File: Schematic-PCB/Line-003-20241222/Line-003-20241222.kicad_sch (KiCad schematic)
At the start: 223 parts, among them J1 VIN, J2 Conn_MD, SW1 RESET, U47 LM393, U48 LM393, U49 LM393, U50 LM393, U51 LM393, U52 LM393, U53 LM393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

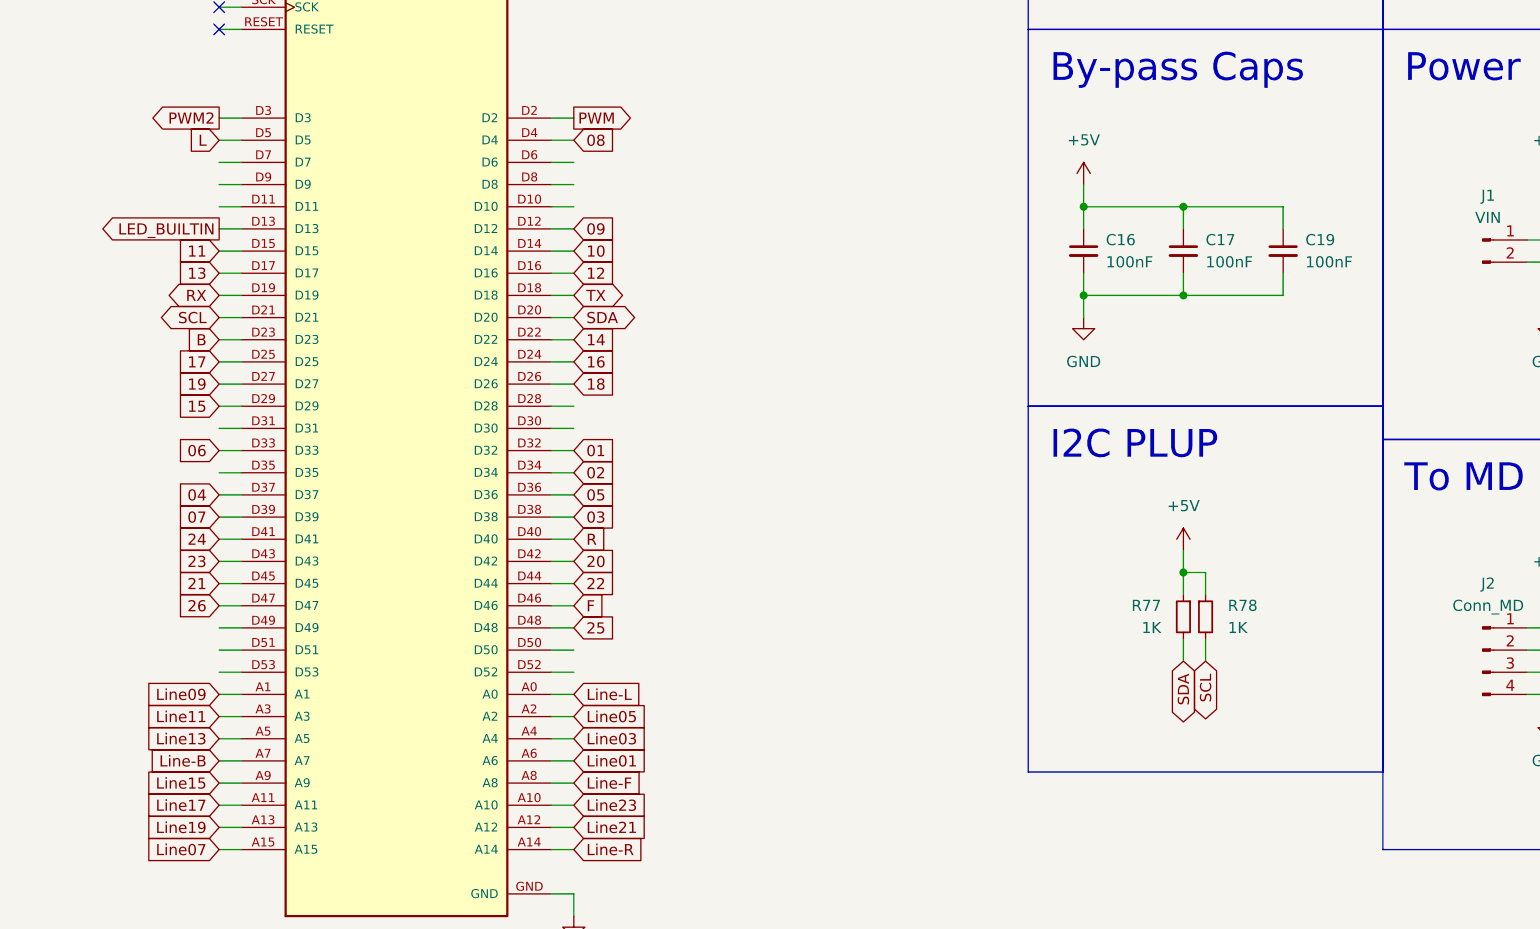
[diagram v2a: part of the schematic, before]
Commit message: update: ラインセンサ基板の2次DRを完了させた
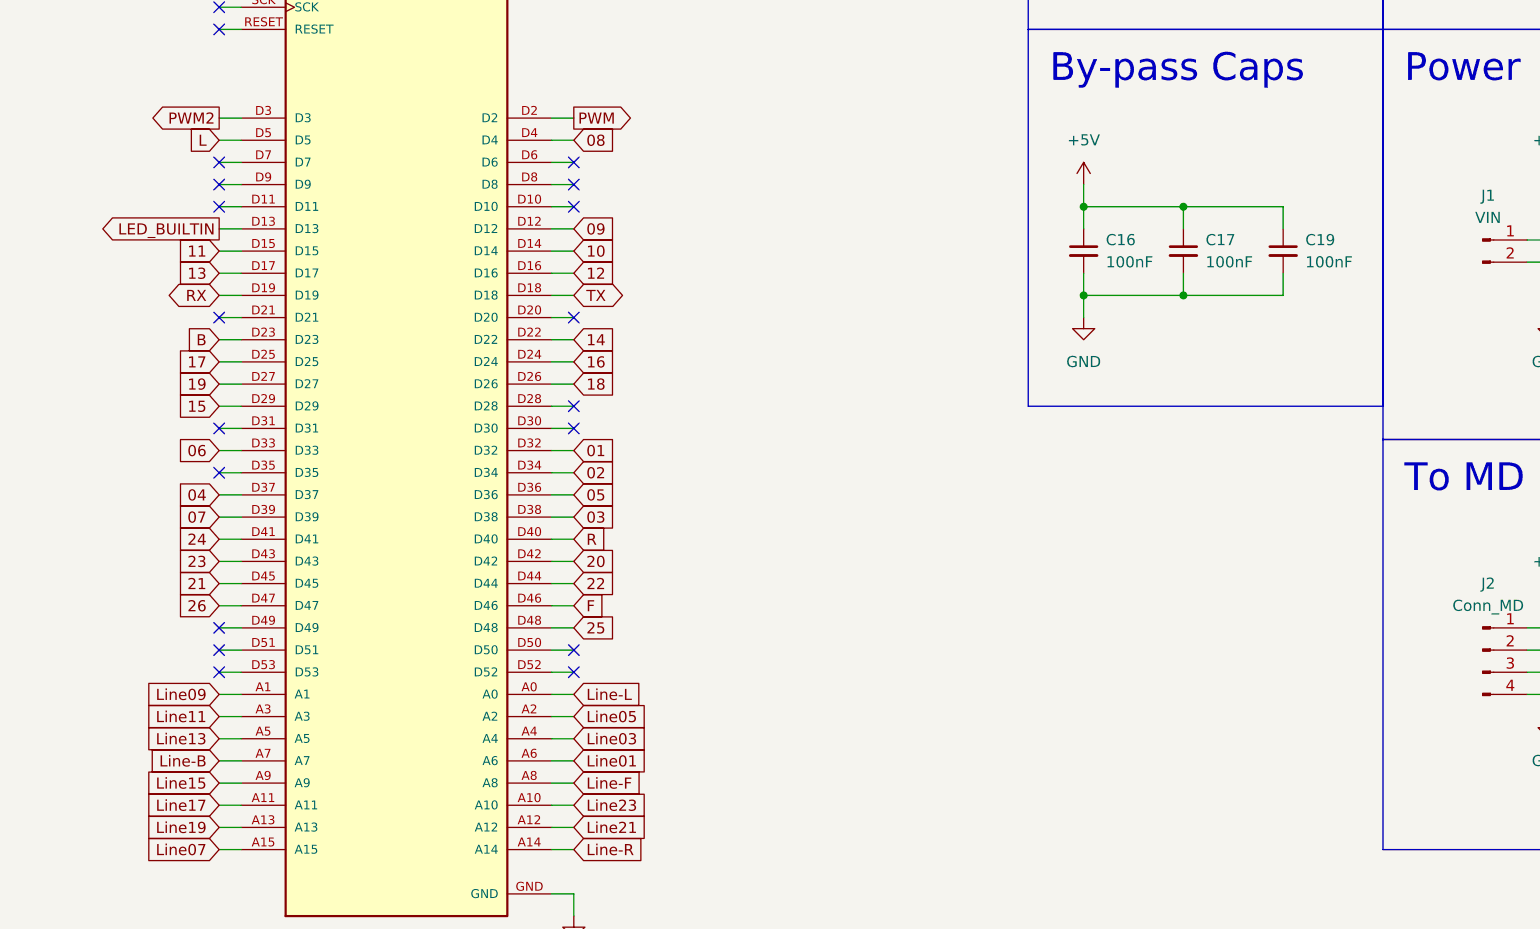
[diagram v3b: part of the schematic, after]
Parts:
- removed R77, R78: 1K, Resistor_SMD:R_0603_1608Metric, symbol Device:R_Small
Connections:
- net SCL: no longer names the net of U62.D21
- net SDA: no longer names the net of U62.D20
- no-connect marks 9 -> 26
